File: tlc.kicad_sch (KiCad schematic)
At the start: 13 parts, among them U2 TL074, U3 TL074, U4 TLC7528

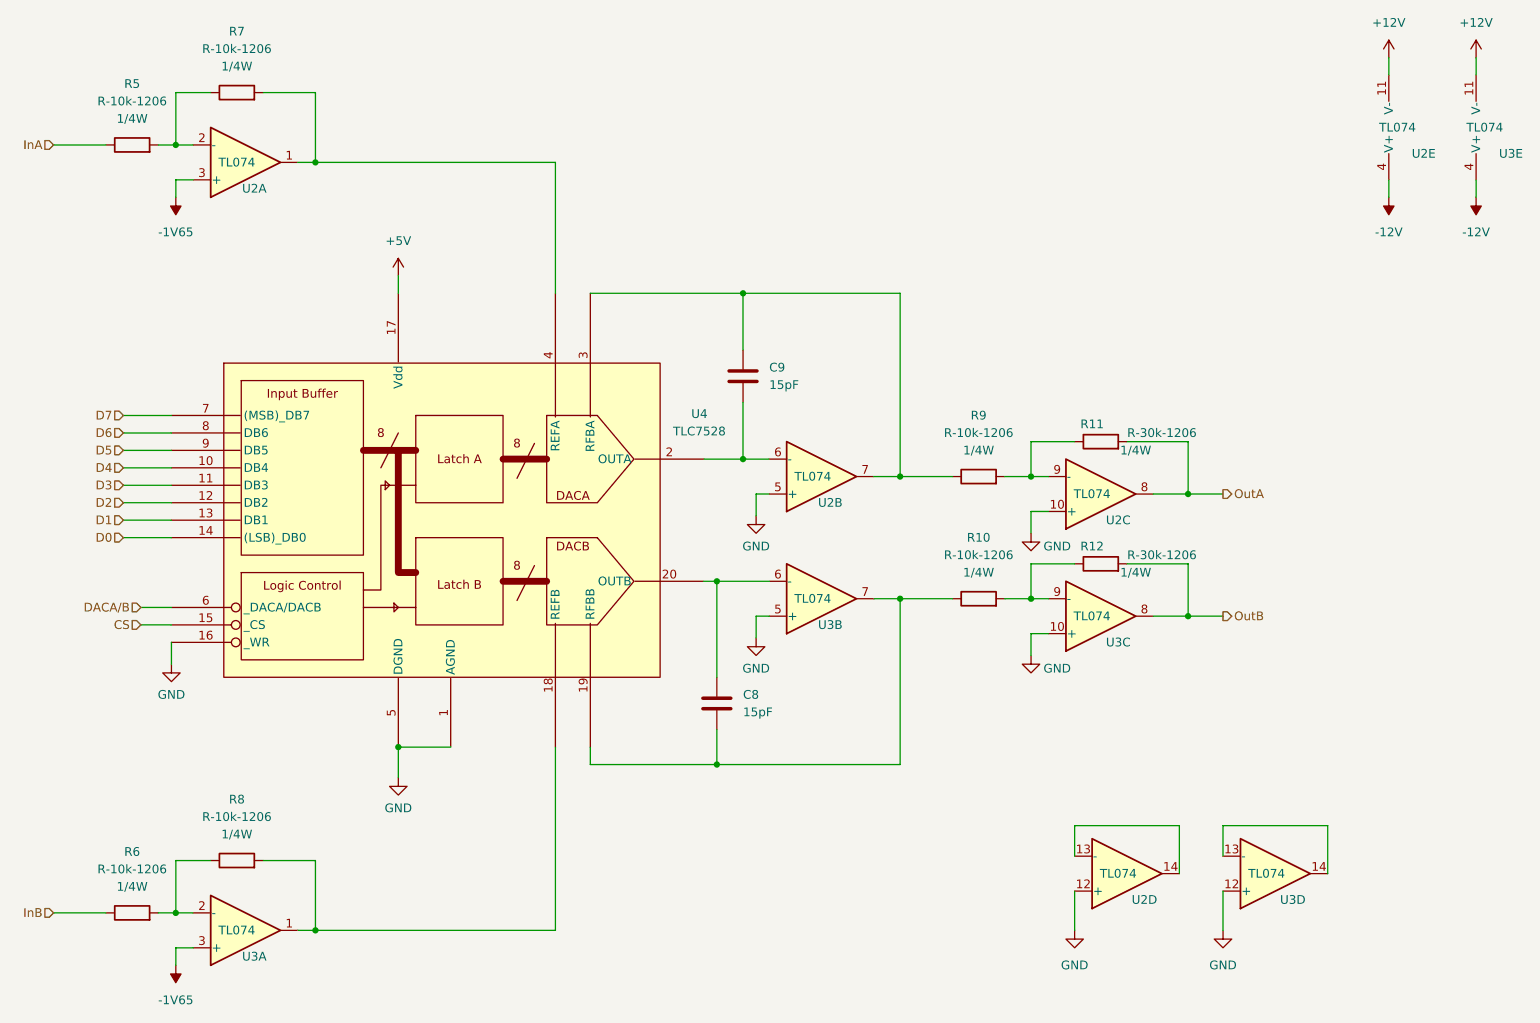
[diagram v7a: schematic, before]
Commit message: reannotated changed to LM324
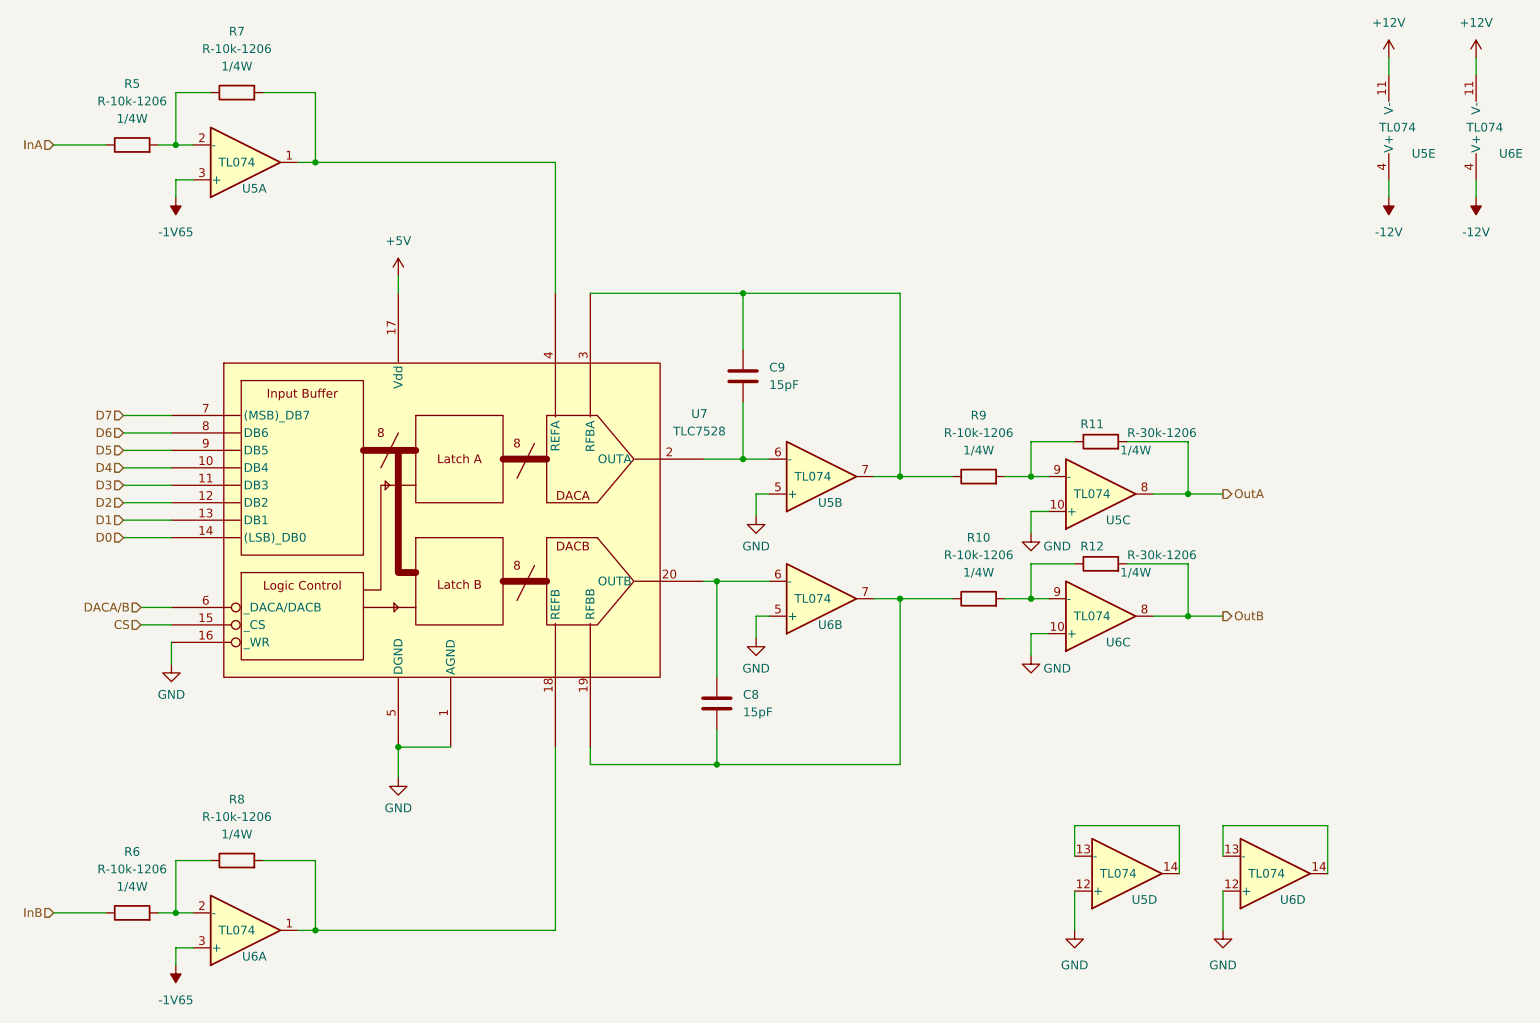
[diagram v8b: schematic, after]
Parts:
- renumbered U2 to U5, U3 to U6, U4 to U7
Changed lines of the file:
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@@
   (symbol (lib_id "eurorack:-1V65") (at 76.2 40.64 180) (unit 1)
     (in_bom yes) (on_board yes) (fields_autoplaced)
-    (property "Reference" "#PWR019" (id 0) (at 76.2 43.18 0)
+    (property "Reference" "#PWR016" (id 0) (at 76.2 43.18 0)
       (effects (font (size 1.27 1.27)) hide)
     )
@@
   (symbol (lib_id "power:GND") (at 228.6 147.32 0) (unit 1)
     (in_bom yes) (on_board yes) (fields_autoplaced)
-    (property "Reference" "#PWR028" (id 0) (at 228.6 153.67 0)
+    (property "Reference" "#PWR025" (id 0) (at 228.6 153.67 0)
       (effects (font (size 1.27 1.27)) hide)
     )
@@
   (symbol (lib_id "power:GND") (at 200.66 107.315 0) (unit 1)
     (in_bom yes) (on_board yes)
-    (property "Reference" "#PWR026" (id 0) (at 200.66 113.665 0)
+    (property "Reference" "#PWR023" (id 0) (at 200.66 113.665 0)
       (effects (font (size 1.27 1.27)) hide)
     )
@@
   (symbol (lib_id "eurorack:TL074") (at 236.22 139.065 0) (mirror x) (unit 4)
     (in_bom yes) (on_board yes)
-    (property "Reference" "U3" (id 0) (at 238.76 142.875 0))
+    (property "Reference" "U6" (id 0) (at 238.76 142.875 0))
     (property "Value" "TL074" (id 1) (at 234.95 139.065 0))
     (property "Footprint" "Package_SO:SO-14_5.3x10.2mm_P1.27mm" (id 2) (at 234.95 141.605 0)
@@
   (symbol (lib_id "eurorack:-1V65") (at 76.2 152.4 180) (unit 1)
     (in_bom yes) (on_board yes) (fields_autoplaced)
-    (property "Reference" "#PWR020" (id 0) (at 76.2 154.94 0)
+    (property "Reference" "#PWR017" (id 0) (at 76.2 154.94 0)
       (effects (font (size 1.27 1.27)) hide)
     )
@@
   (symbol (lib_id "eurorack:TL074") (at 267.97 30.48 0) (mirror x) (unit 5)
     (in_bom yes) (on_board yes)
-    (property "Reference" "U3" (id 0) (at 270.51 34.29 0))
+    (property "Reference" "U6" (id 0) (at 270.51 34.29 0))
     (property "Value" "TL074" (id 1) (at 266.7 30.48 0))
     (property "Footprint" "Package_SO:SO-14_5.3x10.2mm_P1.27mm" (id 2) (at 266.7 33.02 0)
@@
   (symbol (lib_id "power:GND") (at 108.585 125.095 0) (unit 1)
     (in_bom yes) (on_board yes) (fields_autoplaced)
-    (property "Reference" "#PWR022" (id 0) (at 108.585 131.445 0)
+    (property "Reference" "#PWR019" (id 0) (at 108.585 131.445 0)
       (effects (font (size 1.27 1.27)) hide)
     )
@@
   (symbol (lib_id "power:+12V") (at 252.73 20.32 0) (unit 1)
     (in_bom yes) (on_board yes) (fields_autoplaced)
-    (property "Reference" "#PWR029" (id 0) (at 252.73 24.13 0)
+    (property "Reference" "#PWR026" (id 0) (at 252.73 24.13 0)
       (effects (font (size 1.27 1.27)) hide)
     )
@@
   (symbol (lib_id "eurorack:TL074") (at 255.27 30.48 0) (mirror x) (unit 5)
     (in_bom yes) (on_board yes)
-    (property "Reference" "U2" (id 0) (at 257.81 34.29 0))
+    (property "Reference" "U5" (id 0) (at 257.81 34.29 0))
     (property "Value" "TL074" (id 1) (at 254 30.48 0))
     (property "Footprint" "Package_SO:SO-14_5.3x10.2mm_P1.27mm" (id 2) (at 254 33.02 0)
@@
   (symbol (lib_id "eurorack:TL074") (at 86.36 35.56 0) (mirror x) (unit 1)
     (in_bom yes) (on_board yes)
-    (property "Reference" "U2" (id 0) (at 87.63 39.37 0))
+    (property "Reference" "U5" (id 0) (at 87.63 39.37 0))
     (property "Value" "TL074" (id 1) (at 85.09 35.56 0))
     (property "Footprint" "Package_SO:SO-14_5.3x10.2mm_P1.27mm" (id 2) (at 85.09 38.1 0)
@@
   (symbol (lib_id "eurorack:TL074") (at 210.82 101.6 0) (mirror x) (unit 3)
     (in_bom yes) (on_board yes)
-    (property "Reference" "U3" (id 0) (at 213.36 105.41 0))
+    (property "Reference" "U6" (id 0) (at 213.36 105.41 0))
     (property "Value" "TL074" (id 1) (at 209.55 101.6 0))
     (property "Footprint" "Package_SO:SO-14_5.3x10.2mm_P1.27mm" (id 2) (at 209.55 104.14 0)
@@
   (symbol (lib_id "eurorack:TLC7528") (at 116.205 87.63 0) (unit 1)
     (in_bom yes) (on_board yes) (fields_autoplaced)
-    (property "Reference" "U4" (id 0) (at 152.4 72.1612 0))
+    (property "Reference" "U7" (id 0) (at 152.4 72.1612 0))
     (property "Value" "TLC7528" (id 1) (at 152.4 74.7012 0))
     (property "Footprint" "Package_SO:SOIC-20W_7.5x12.8mm_P1.27mm" (id 2) (at 116.205 87.63 0)
@@
   (symbol (lib_id "eurorack:TL074") (at 170.18 99.06 0) (mirror x) (unit 2)
     (in_bom yes) (on_board yes)
-    (property "Reference" "U3" (id 0) (at 171.45 102.87 0))
+    (property "Reference" "U6" (id 0) (at 171.45 102.87 0))
     (property "Value" "TL074" (id 1) (at 168.91 99.06 0))
     (property "Footprint" "Package_SO:SO-14_5.3x10.2mm_P1.27mm" (id 2) (at 168.91 101.6 0)
@@
   (symbol (lib_id "eurorack:TL074") (at 214.63 139.065 0) (mirror x) (unit 4)
     (in_bom yes) (on_board yes)
-    (property "Reference" "U2" (id 0) (at 217.17 142.875 0))
+    (property "Reference" "U5" (id 0) (at 217.17 142.875 0))
     (property "Value" "TL074" (id 1) (at 213.36 139.065 0))
     (property "Footprint" "Package_SO:SO-14_5.3x10.2mm_P1.27mm" (id 2) (at 213.36 141.605 0)
@@
   (symbol (lib_id "power:GND") (at 160.655 104.775 0) (unit 1)
     (in_bom yes) (on_board yes) (fields_autoplaced)
-    (property "Reference" "#PWR024" (id 0) (at 160.655 111.125 0)
+    (property "Reference" "#PWR021" (id 0) (at 160.655 111.125 0)
       (effects (font (size 1.27 1.27)) hide)
     )
@@
   (symbol (lib_id "eurorack:TL074") (at 86.36 147.32 0) (mirror x) (unit 1)
     (in_bom yes) (on_board yes)
-    (property "Reference" "U3" (id 0) (at 87.63 151.13 0))
+    (property "Reference" "U6" (id 0) (at 87.63 151.13 0))
     (property "Value" "TL074" (id 1) (at 85.09 147.32 0))
     (property "Footprint" "Package_SO:SO-14_5.3x10.2mm_P1.27mm" (id 2) (at 85.09 149.86 0)
@@
   (symbol (lib_id "power:GND") (at 75.565 108.585 0) (unit 1)
     (in_bom yes) (on_board yes) (fields_autoplaced)
-    (property "Reference" "#PWR018" (id 0) (at 75.565 114.935 0)
+    (property "Reference" "#PWR015" (id 0) (at 75.565 114.935 0)
       (effects (font (size 1.27 1.27)) hide)
     )
@@
   (symbol (lib_id "power:GND") (at 200.66 89.535 0) (unit 1)
     (in_bom yes) (on_board yes)
-    (property "Reference" "#PWR025" (id 0) (at 200.66 95.885 0)
+    (property "Reference" "#PWR022" (id 0) (at 200.66 95.885 0)
       (effects (font (size 1.27 1.27)) hide)
     )
@@
   (symbol (lib_id "eurorack:TL074") (at 170.18 81.28 0) (mirror x) (unit 2)
     (in_bom yes) (on_board yes)
-    (property "Reference" "U2" (id 0) (at 171.45 85.09 0))
+    (property "Reference" "U5" (id 0) (at 171.45 85.09 0))
     (property "Value" "TL074" (id 1) (at 168.91 81.28 0))
     (property "Footprint" "Package_SO:SO-14_5.3x10.2mm_P1.27mm" (id 2) (at 168.91 83.82 0)
@@
   (symbol (lib_id "power:-12V") (at 252.73 40.64 180) (unit 1)
     (in_bom yes) (on_board yes) (fields_autoplaced)
-    (property "Reference" "#PWR030" (id 0) (at 252.73 43.18 0)
+    (property "Reference" "#PWR027" (id 0) (at 252.73 43.18 0)
       (effects (font (size 1.27 1.27)) hide)
     )
@@
   (symbol (lib_id "power:GND") (at 207.01 147.32 0) (unit 1)
     (in_bom yes) (on_board yes) (fields_autoplaced)
-    (property "Reference" "#PWR027" (id 0) (at 207.01 153.67 0)
+    (property "Reference" "#PWR024" (id 0) (at 207.01 153.67 0)
       (effects (font (size 1.27 1.27)) hide)
     )
@@
   (symbol (lib_id "eurorack:TL074") (at 210.82 83.82 0) (mirror x) (unit 3)
     (in_bom yes) (on_board yes)
-    (property "Reference" "U2" (id 0) (at 213.36 87.63 0))
+    (property "Reference" "U5" (id 0) (at 213.36 87.63 0))
     (property "Value" "TL074" (id 1) (at 209.55 83.82 0))
     (property "Footprint" "Package_SO:SO-14_5.3x10.2mm_P1.27mm" (id 2) (at 209.55 86.36 0)
@@
   (symbol (lib_id "power:+5V") (at 108.585 52.07 0) (unit 1)
     (in_bom yes) (on_board yes) (fields_autoplaced)
-    (property "Reference" "#PWR021" (id 0) (at 108.585 55.88 0)
+    (property "Reference" "#PWR018" (id 0) (at 108.585 55.88 0)
       (effects (font (size 1.27 1.27)) hide)
     )
@@
   (symbol (lib_id "power:-12V") (at 265.43 40.64 180) (unit 1)
     (in_bom yes) (on_board yes) (fields_autoplaced)
-    (property "Reference" "#PWR032" (id 0) (at 265.43 43.18 0)
+    (property "Reference" "#PWR029" (id 0) (at 265.43 43.18 0)
       (effects (font (size 1.27 1.27)) hide)
     )
@@
   (symbol (lib_id "power:GND") (at 160.655 86.995 0) (unit 1)
     (in_bom yes) (on_board yes) (fields_autoplaced)
-    (property "Reference" "#PWR023" (id 0) (at 160.655 93.345 0)
+    (property "Reference" "#PWR020" (id 0) (at 160.655 93.345 0)
       (effects (font (size 1.27 1.27)) hide)
     )
@@
   (symbol (lib_id "power:+12V") (at 265.43 20.32 0) (unit 1)
     (in_bom yes) (on_board yes) (fields_autoplaced)
-    (property "Reference" "#PWR031" (id 0) (at 265.43 24.13 0)
-      (effects (font (size 1.27 1.27)) hide)
-    )
+    (property "Reference" "#PWR028" (id 0) (at 265.43 24.13 0)
+      (effects (font (size 1.27 1.27)) hide)
+    )
